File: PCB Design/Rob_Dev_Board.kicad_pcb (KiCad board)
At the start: 2 copper layers, 59 x 40 mm, 2 parts, among them U1 DRV8245HQRXZRQ1, U2 ESP32-S3-WROOM-1U-N16R8

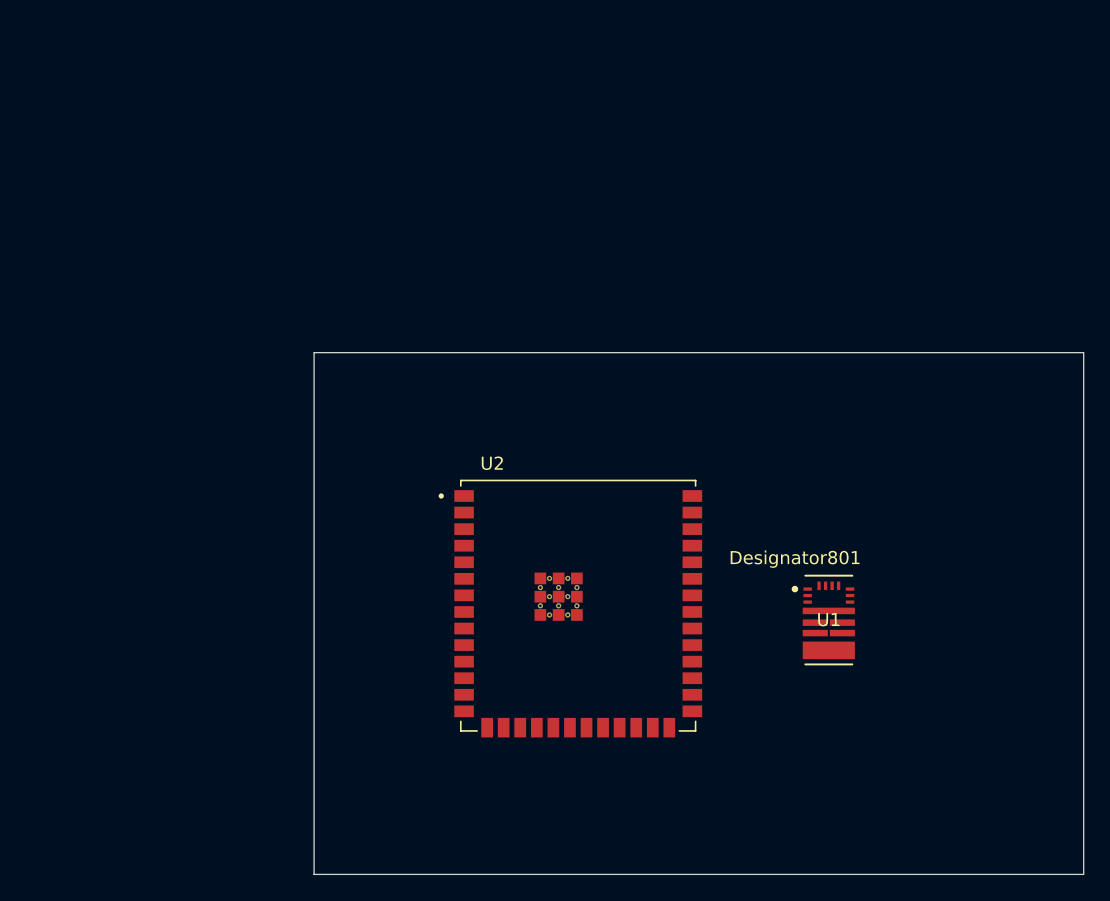
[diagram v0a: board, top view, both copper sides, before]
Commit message: Added some more components to PCB design, added datasheet for possible BLDC motor driver
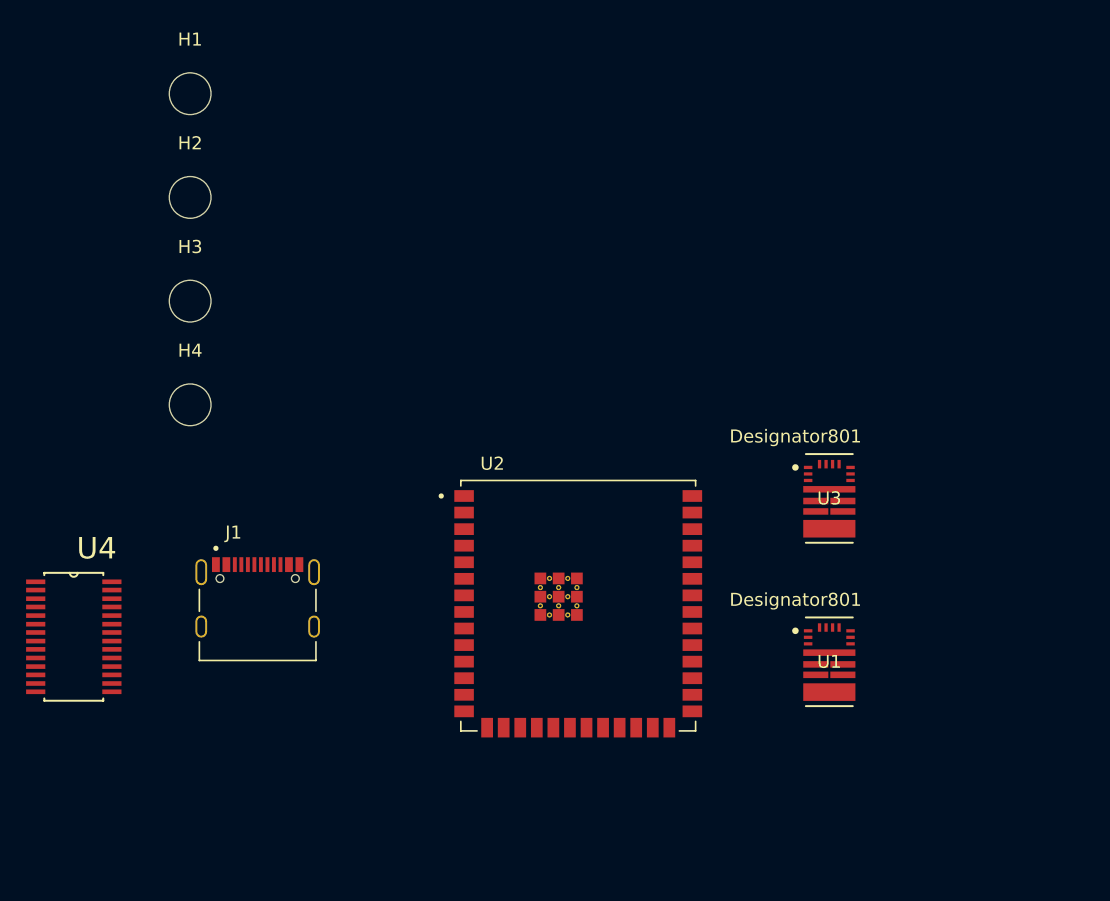
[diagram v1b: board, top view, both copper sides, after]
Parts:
- added H1: MountingHole, MountingHole:MountingHole_3.2mm_M3, F.Cu at (54.5, 40.6)
- added H2: MountingHole, MountingHole:MountingHole_3.2mm_M3, F.Cu at (54.5, 48.6)
- added H3: MountingHole, MountingHole:MountingHole_3.2mm_M3, F.Cu at (54.5, 56.5)
- added H4: MountingHole, MountingHole:MountingHole_3.2mm_M3, F.Cu at (54.5, 64.5)
- added J1: TYPE-C-31-M-12, Type C Connector:HRO_TYPE-C-31-M-12, F.Cu at (59.7, 81.5)
- added U3: DRV8245HQRXZRQ1, DRV8245H-Q1:RXZ0016A-MFG, F.Cu at (103.5, 71.7)
- added U4: PCA9685PW_118, PCA9685 PWM Servo Driver:SOP65P640X110-28N, F.Cu at (45.6, 82.3)
- moved U1 3.20 mm to (103.5, 84.2)
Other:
- board outline removed
- copper layers 2 -> 4
